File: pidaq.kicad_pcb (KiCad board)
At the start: 2 copper layers, 83.8 x 78.1 mm, 41 parts, among them J1 Screw_Terminal_01x08, J2 Screw_Terminal_01x08, J3 Screw_Terminal_01x10, J4 Screw_Terminal_01x10, J5 Conn_01x02_Male, J6 Conn_01x08_Female, U1 LTC2984CLX-DNP, U2 LTC2418IGN-DNP

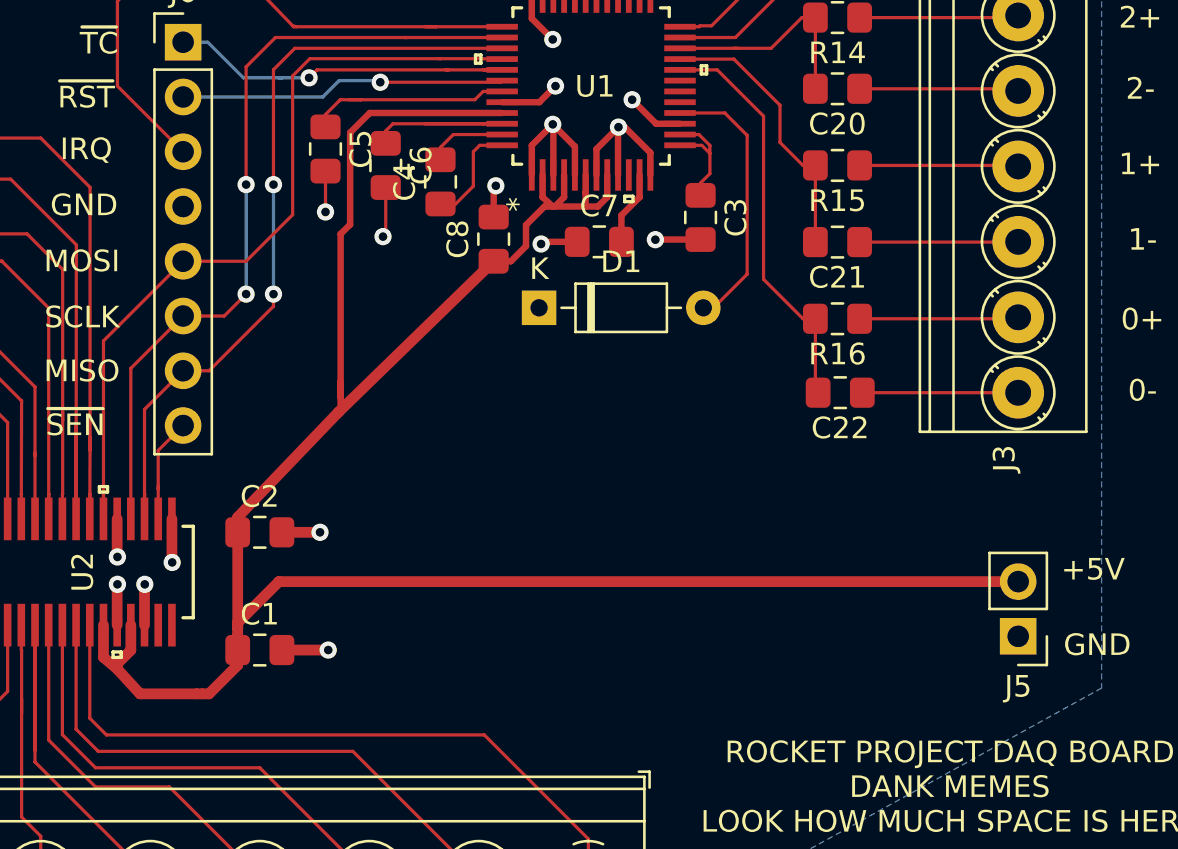
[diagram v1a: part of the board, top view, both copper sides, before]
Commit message: add level shifters to MISO
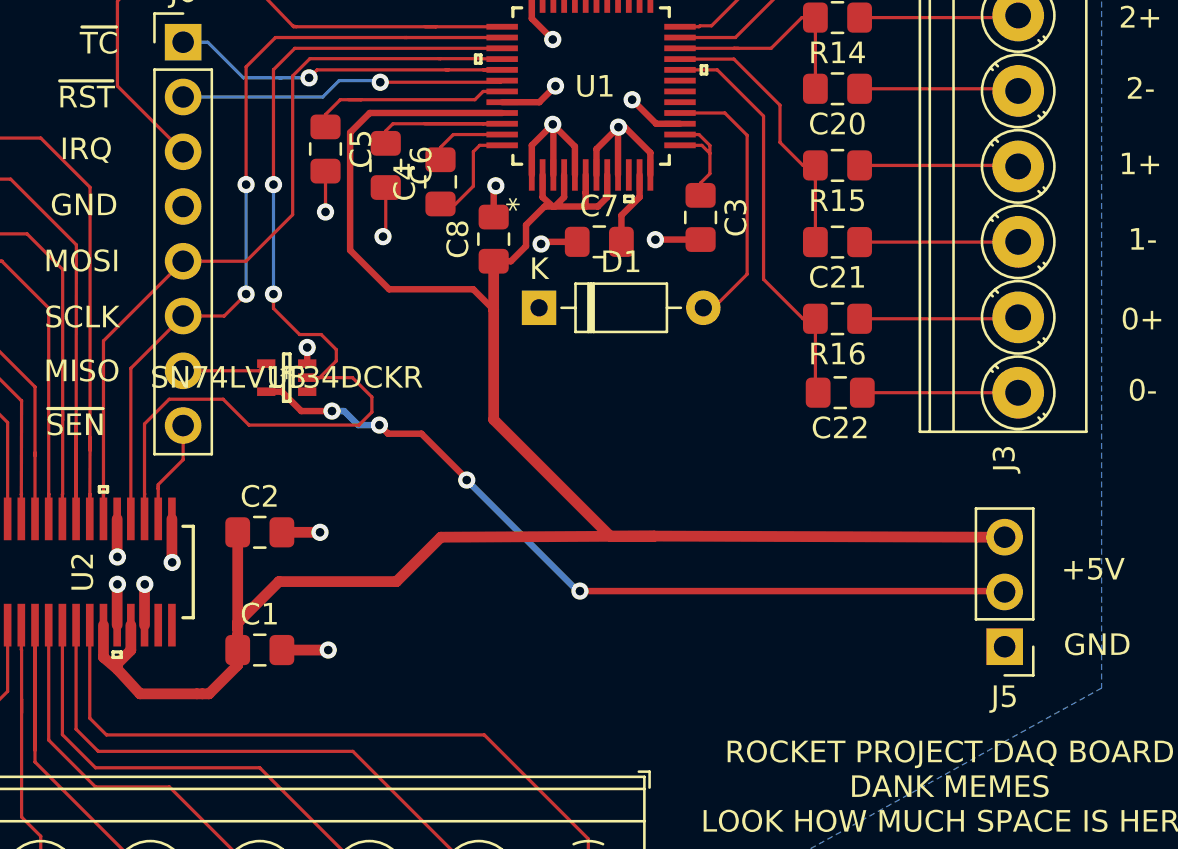
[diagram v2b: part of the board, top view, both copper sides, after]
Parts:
- added U3: SN74LV1T34DCKR, proj_footprints:SN74LV1T34DCKR, F.Cu at (117.2, 127.7)
- C2, C7, C8: value 0.1uF -> 100nF
- C4: value 10uF X7R -> 10uF
- C6: value 10uF X5R -> 10uF
- J5: value Conn_01x02_Male -> Conn_01x03_Male; footprint Connector_PinHeader_2.54mm:PinHeader_1x02_P2.54mm_Vertical -> Connector_PinHeader_2.54mm:PinHeader_1x03_P2.54mm_Vertical
- moved J5 0.79 mm to (150.5, 140.2)
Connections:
- J5 pad 2: +5V -> VDOUT
- J6 pad 7: MISO -> Net-(J6-Pad7)
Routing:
- net VDOUT: track 0.00 -> 38.8 mm, vias 0 -> 4
- net MISO: track 35.2 -> 48.3 mm
- net Net-(J6-Pad7): track 0.00 -> 3.99 mm
- net +5V: track 107.2 -> 105.5 mm
- net GND: track 116.4 -> 117.4 mm, vias 16 -> 17

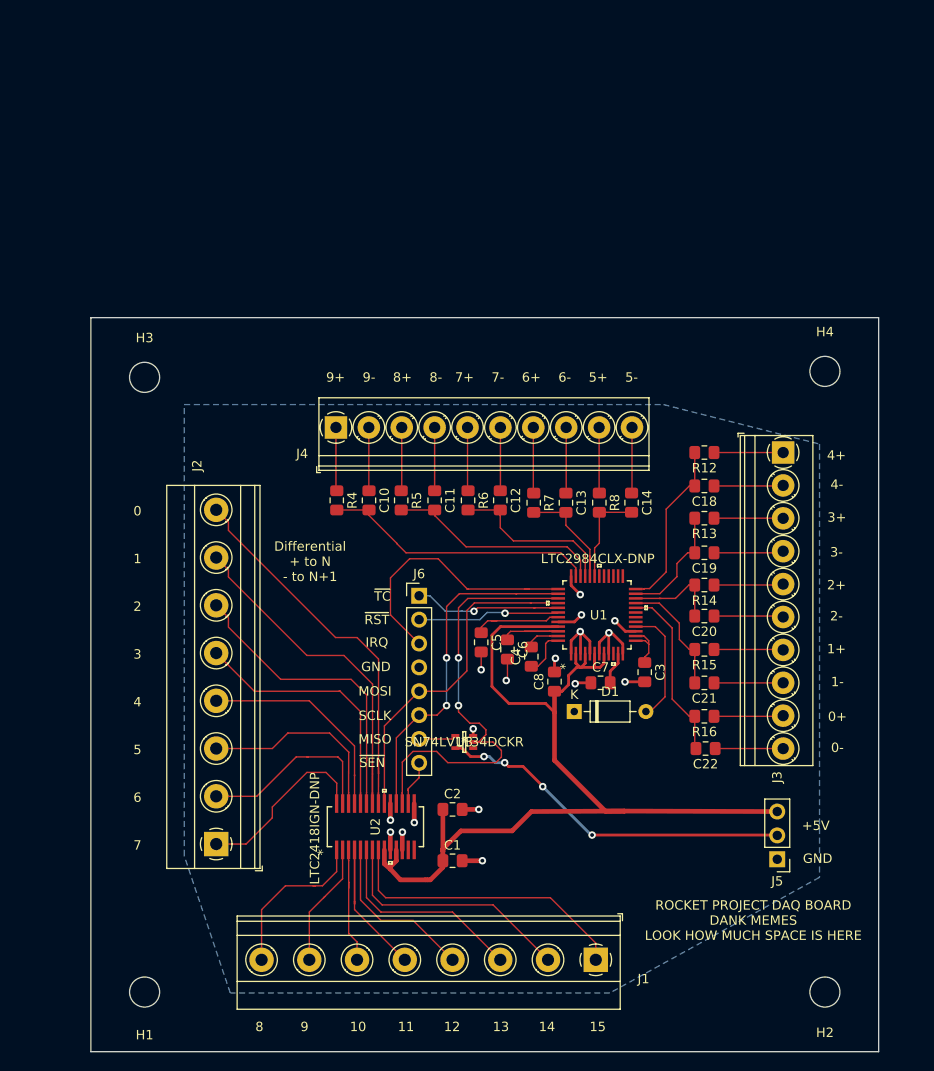
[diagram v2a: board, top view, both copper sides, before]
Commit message: reversed screw terminal symbols
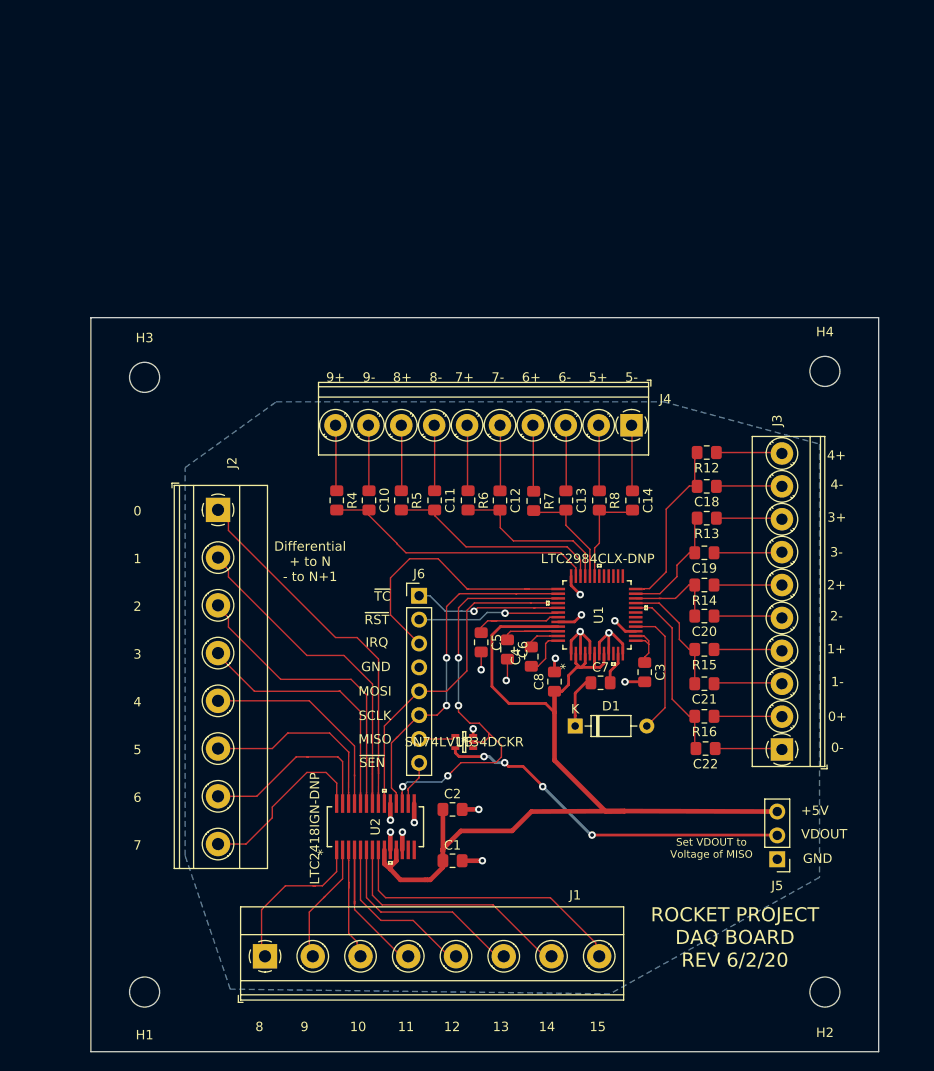
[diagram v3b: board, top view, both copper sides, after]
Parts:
- moved J2 35.6 mm to (91.0, 103.0), turned to 270 degrees
- moved J1 35.2 mm to (96.0, 150.5), turned to 0 degrees
- moved J3 31.6 mm to (151.0, 128.5), turned to 90 degrees
- moved J4 31.5 mm to (135.0, 94.0), turned to 180 degrees
- moved D1 1.54 mm to (129.0, 126.0)
- moved C18 0.26 mm to (143.0, 100.5)
- moved C14 0.26 mm to (135.1, 102.0)
- moved R12 0.25 mm to (143.0, 96.9)
- moved R13 0.25 mm to (143.0, 103.9)
- moved C13 0.24 mm to (128.0, 102.0)
- moved R8 0.23 mm to (131.6, 102.0)
- moved R7 0.19 mm to (124.6, 102.0)
- moved C21 0.09 mm to (142.7, 121.5)
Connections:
- net CS_SEN renamed ~SEN
- net CS_TC renamed ~TC
- net Net-(J6-Pad7) renamed /MISO_SAFE
- J1 pad 1: SEN15 -> Net-(J1-Pad1)
- J1 pad 2: SEN14 -> Net-(J1-Pad2)
- J1 pad 3: SEN13 -> Net-(J1-Pad3)
- J1 pad 4: SEN12 -> Net-(J1-Pad4)
- J1 pad 5: SEN11 -> Net-(J1-Pad5)
- J1 pad 6: SEN10 -> Net-(J1-Pad6)
- J1 pad 7: SEN9 -> Net-(J1-Pad7)
- J1 pad 8: SEN8 -> Net-(J1-Pad8)
- J2 pad 1: /SEN7 -> /SEN0
- J2 pad 2: /SEN6 -> /SEN1
- J2 pad 3: /SEN5 -> /SEN2
- J2 pad 4: /SEN4 -> /SEN3
- J2 pad 5: /SEN3 -> /SEN4
- J2 pad 6: /SEN2 -> /SEN5
- J2 pad 7: /SEN1 -> /SEN6
- J2 pad 8: /SEN0 -> /SEN7
- J3 pad 1: Net-(J3-Pad1) -> GND
- J3 pad 10: GND -> Net-(J3-Pad10)
- J3 pad 2: GND -> Net-(J3-Pad2)
- J3 pad 3: Net-(J3-Pad3) -> GND
- J3 pad 4: GND -> Net-(J3-Pad4)
- J3 pad 5: Net-(J3-Pad5) -> GND
- J3 pad 6: GND -> Net-(J3-Pad6)
- J3 pad 7: Net-(J3-Pad7) -> GND
- J3 pad 8: GND -> Net-(J3-Pad8)
- J3 pad 9: Net-(J3-Pad9) -> GND
- J4 pad 1: Net-(J4-Pad1) -> GND
- J4 pad 10: GND -> Net-(J4-Pad10)
- J4 pad 2: GND -> Net-(J4-Pad2)
- J4 pad 3: Net-(J4-Pad3) -> GND
- J4 pad 4: GND -> Net-(J4-Pad4)
- J4 pad 5: Net-(J4-Pad5) -> GND
- J4 pad 6: GND -> Net-(J4-Pad6)
- J4 pad 7: Net-(J4-Pad7) -> GND
- J4 pad 8: GND -> Net-(J4-Pad8)
- J4 pad 9: Net-(J4-Pad9) -> GND
- R12 pad 1: Net-(J3-Pad1) -> Net-(J3-Pad10)
- R13 pad 1: Net-(J3-Pad3) -> Net-(J3-Pad8)
- R14 pad 1: Net-(J3-Pad5) -> Net-(J3-Pad6)
- R15 pad 1: Net-(J3-Pad7) -> Net-(J3-Pad4)
- R16 pad 1: Net-(J3-Pad9) -> Net-(J3-Pad2)
- R4 pad 1: Net-(J4-Pad1) -> Net-(J4-Pad10)
- R5 pad 1: Net-(J4-Pad3) -> Net-(J4-Pad8)
- R6 pad 1: Net-(J4-Pad5) -> Net-(J4-Pad6)
- R7 pad 1: Net-(J4-Pad7) -> Net-(J4-Pad4)
- R8 pad 1: Net-(J4-Pad9) -> Net-(J4-Pad2)
- U2 pad 1: SEN8 -> Net-(J1-Pad1)
- U2 pad 2: SEN9 -> Net-(J1-Pad2)
- U2 pad 3: SEN10 -> Net-(J1-Pad3)
- U2 pad 4: SEN11 -> Net-(J1-Pad4)
- U2 pad 5: SEN12 -> Net-(J1-Pad5)
- U2 pad 6: SEN13 -> Net-(J1-Pad6)
- U2 pad 7: SEN14 -> Net-(J1-Pad7)
- U2 pad 8: SEN15 -> Net-(J1-Pad8)
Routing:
- net SEN15: track 31.5 -> 0.00 mm
- net Net-(J1-Pad8): track 0.00 -> 31.5 mm
- net SEN14: track 26.4 -> 0.00 mm
- net Net-(J1-Pad7): track 0.00 -> 26.4 mm
- net SEN13: track 22.1 -> 0.00 mm
- net Net-(J1-Pad6): track 0.00 -> 22.1 mm
- net SEN11: track 20.0 -> 0.00 mm
- net Net-(J1-Pad4): track 0.00 -> 20.0 mm
- net SEN12: track 17.8 -> 0.00 mm
- net Net-(J1-Pad5): track 0.00 -> 17.8 mm
- net SEN8: track 17.6 -> 0.00 mm
- net Net-(J1-Pad1): track 0.00 -> 17.6 mm
- net SEN9: track 13.3 -> 0.00 mm
- net Net-(J1-Pad2): track 0.00 -> 13.3 mm
- net SEN10: track 12.7 -> 0.00 mm
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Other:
- board text added: "ROCKET PROJECT DAQ BOARD REV 6/2/20"
- board text added: "Set VDOUT to Voltage of MISO"
- board text added: "VDOUT"
- board text removed: "ROCKET PROJECT DAQ BOARD DANK MEMES LOOK HOW MUCH SPACE IS HERE"

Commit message: turn screw holes into plated ones for more grounding
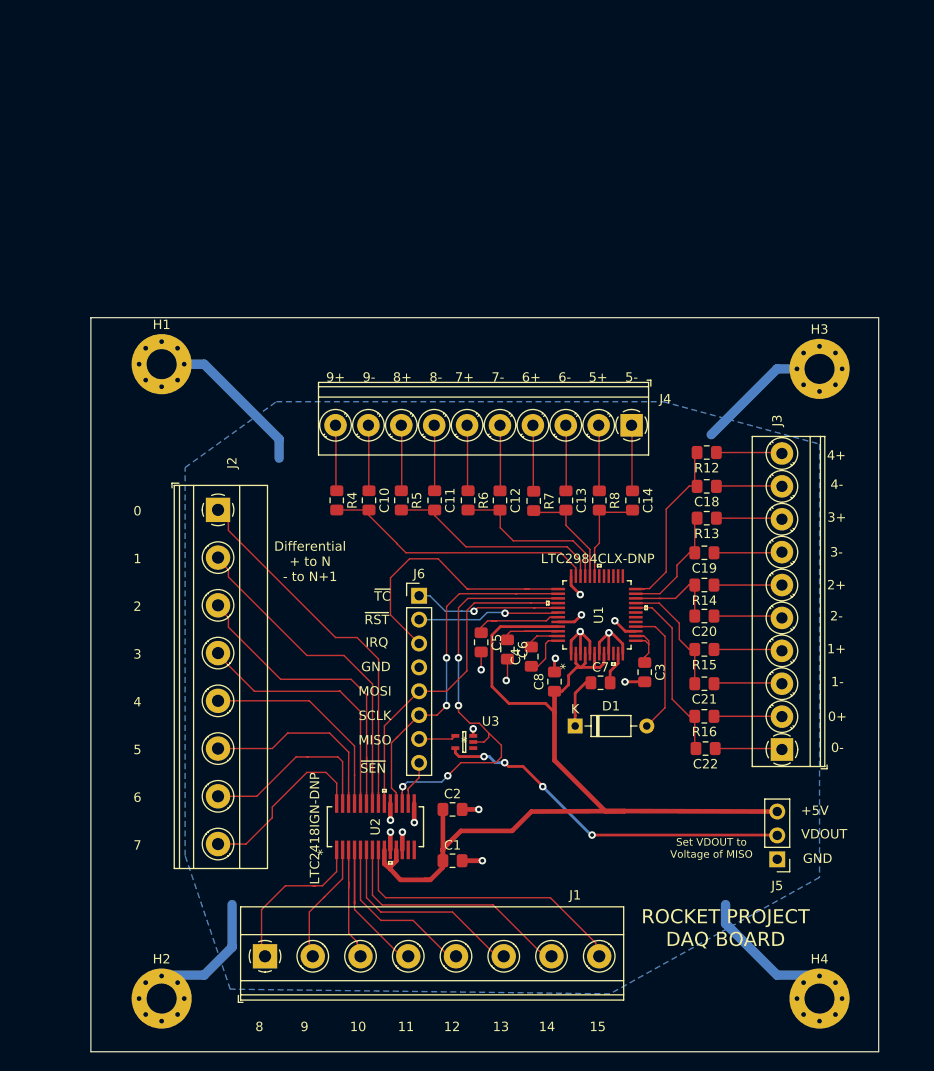
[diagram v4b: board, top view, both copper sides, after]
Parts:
- H1, H2, H3, H4: value MountingHole -> MountingHole_Pad; footprint MountingHole:MountingHole_3.2mm_M3 -> MountingHole:MountingHole_3.2mm_M3_Pad_Via
- moved H3 71.8 mm to (155.0, 88.0)
- moved H2 70.6 mm to (85.0, 155.0)
- moved H1 66.8 mm to (85.0, 87.5)
- moved H4 66.7 mm to (155.0, 155.0)
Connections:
- H1 pad 1: (no net) -> GND
- H2 pad 1: (no net) -> GND
- H3 pad 1: (no net) -> GND
- H4 pad 1: (no net) -> GND
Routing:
- net GND: track 121.3 -> 181.1 mm
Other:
- board text added: "ROCKET PROJECT DAQ BOARD"
- board text removed: "ROCKET PROJECT DAQ BOARD REV 6/2/20"

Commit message: completed design 2.0
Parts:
- removed C19, C20, C21, C22: 100pF, Capacitor_SMD:C_0805_2012Metric_Pad1.15x1.40mm_HandSolder
- removed R12, R13, R14, R15, R16: 100, Resistor_SMD:R_0805_2012Metric_Pad1.15x1.40mm_HandSolder
- added C15: 10uF, Capacitor_SMD:C_0805_2012Metric_Pad1.15x1.40mm_HandSolder, F.Cu at (105.2, 110.4)
- added C16: 10uF, Capacitor_SMD:C_0805_2012Metric_Pad1.15x1.40mm_HandSolder, F.Cu at (104.4, 107.1)
- added C17: 10uF, Capacitor_SMD:C_0805_2012Metric_Pad1.15x1.40mm_HandSolder, F.Cu at (128.1, 80.3)
- added C9: 100pF, Capacitor_SMD:C_0805_2012Metric_Pad1.15x1.40mm_HandSolder, F.Cu at (85.1, 124.5)
- added J7: Screw_Terminal_01x04, TerminalBlock_Phoenix:TerminalBlock_Phoenix_MKDS-1,5-4-5.08_1x04_P5.08mm_Horizontal, F.Cu at (133.3, 136.5)
- added J8: Conn_01x03_Male, Connector_PinHeader_2.54mm:PinHeader_1x03_P2.54mm_Vertical, F.Cu at (138.8, 111.6)
- added R1: 100, Resistor_SMD:R_0805_2012Metric_Pad1.15x1.40mm_HandSolder, F.Cu at (85.1, 92.7)
- added R10: 100, Resistor_SMD:R_0805_2012Metric_Pad1.15x1.40mm_HandSolder, F.Cu at (85.1, 106.7)
- added R2: 100, Resistor_SMD:R_0805_2012Metric_Pad1.15x1.40mm_HandSolder, F.Cu at (85.1, 87.6)
- added R3: 100, Resistor_SMD:R_0805_2012Metric_Pad1.15x1.40mm_HandSolder, F.Cu at (85.1, 82.5)
- added R9: 100, Resistor_SMD:R_0805_2012Metric_Pad1.15x1.40mm_HandSolder, F.Cu at (85.1, 111.8)
- added RG1: R_US, Resistor_THT:R_Axial_DIN0204_L3.6mm_D1.6mm_P7.62mm_Horizontal, F.Cu at (138.0, 120.8)
- added U4: INA126U, footprints:INA126U, F.Cu at (145.8, 124.8)
- C1: value 10uF -> 100nF
- C14: value 100pF -> 10uF
- C18: value 100pF -> 0.1uF
- C2: value 100nF -> 1uF
- C3: value 1uF -> 100nF
- C4, C5, C6: value 10uF -> 100pF
- C7, C8: value 100nF -> 100pF
- J1, J2: value Screw_Terminal_01x08 -> Screw_Terminal_01x10; footprint TerminalBlock_Phoenix:TerminalBlock_Phoenix_MKDS-1,5-8-5.08_1x08_P5.08mm_Horizontal -> TerminalBlock_Phoenix:TerminalBlock_Phoenix_MPT-0,5-10-2.54_1x10_P2.54mm_Horizontal
- J3, J4: value Screw_Terminal_01x10 -> Screw_Terminal_01x08; footprint TerminalBlock_Phoenix:TerminalBlock_Phoenix_PT-1,5-10-3.5-H_1x10_P3.50mm_Horizontal -> TerminalBlock_Phoenix:TerminalBlock_Phoenix_MKDS-1,5-8-5.08_1x08_P5.08mm_Horizontal
- U1: footprint proj_footprints:LTC2984CLX-PBF -> footprints:LTC2984CLX-PBF
- U2: value LTC2418IGN-DNP -> LTC2449CUHF; footprint proj_footprints:LTC2418IGN-PBF -> footprints:LTC2449CUHF
- U3: footprint proj_footprints:SN74LV1T34DCKR -> footprints:SN74LV1T34DCKR
- moved H2 122.5 mm to (158.8, 57.1)
- moved H4 80.3 mm to (76.2, 139.7)
- moved C8 66.2 mm to (85.1, 69.8), turned to 0 degrees
- moved C7 65.8 mm to (85.1, 74.9)
- moved U2 65.7 mm to (133.3, 76.2), turned to 180 degrees
- moved J1 60.3 mm to (78.7, 92.7), turned to 90 degrees
- moved D1 58.2 mm to (78.0, 98.0)
- moved J5 55.4 mm to (95.1, 139.4), turned to 90 degrees
- moved C6 52.7 mm to (85.1, 80.0), turned to 0 degrees
- moved H3 51.8 mm to (158.8, 139.7)
- moved R8 48.8 mm to (85.1, 116.8), turned to 0 degrees
- moved C4 48.5 mm to (85.1, 90.2), turned to 0 degrees
- moved C5 46.6 mm to (85.1, 85.1), turned to 0 degrees
- moved C1 44.8 mm to (107.8, 96.3), turned to 270 degrees
- moved R7 44.2 mm to (85.1, 121.9), turned to 0 degrees
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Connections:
- C1 pad 1: +5V -> GND
- C1 pad 2: GND -> Net-(C1-Pad2)
- C10 pad 2: TC9+ -> TC8+
- C11 pad 2: TC8+ -> TC7+
- C12 pad 2: TC7+ -> TC6+
- C13 pad 2: TC6+ -> TC5+
- C14 pad 1: GND -> Net-(C14-Pad1)
- C14 pad 2: TC5+ -> Net-(C14-Pad2)
- C18 pad 1: GND -> +5V
- C18 pad 2: TC4+ -> GND
- C2 pad 1: +5V -> Net-(C2-Pad1)
- C3 pad 1: Net-(C3-Pad1) -> +5V
- C4 pad 1: Net-(C4-Pad1) -> GND
- C4 pad 2: Net-(C4-Pad2) -> TC4+
- C5 pad 1: Net-(C5-Pad1) -> GND
- C5 pad 2: GND -> TC3+
- C6 pad 1: Net-(C6-Pad1) -> GND
- C6 pad 2: GND -> TC2+
- C7 pad 2: Net-(C7-Pad2) -> TC1+
- C8 pad 1: +5V -> GND
- C8 pad 2: GND -> TC0+
- D1 pad 2: Net-(D1-Pad2) -> /thermocouples/CJ
- J1 pad 1: Net-(J1-Pad1) -> /thermocouples/TC4RAW
- J1 pad 2: Net-(J1-Pad2) -> GND
- J1 pad 3: Net-(J1-Pad3) -> /thermocouples/TC3RAQ
- J1 pad 4: Net-(J1-Pad4) -> GND
- J1 pad 5: Net-(J1-Pad5) -> /thermocouples/TC2RAW
- J1 pad 6: Net-(J1-Pad6) -> GND
- J1 pad 7: Net-(J1-Pad7) -> /thermocouples/TC1RAW
- J1 pad 8: Net-(J1-Pad8) -> GND
- J2 pad 1: /SEN0 -> /thermocouples/TC9RAW
- J2 pad 2: /SEN1 -> GND
- J2 pad 3: /SEN2 -> /thermocouples/TC8RAW
- J2 pad 4: /SEN3 -> GND
- J2 pad 5: /SEN4 -> /thermocouples/TC7RAW
- J2 pad 6: /SEN5 -> GND
- J2 pad 7: /SEN6 -> /thermocouples/TC6RAW
- J2 pad 8: /SEN7 -> GND
- J3 pad 1: GND -> SEN0
- J3 pad 2: Net-(J3-Pad2) -> SEN1
- J3 pad 3: GND -> SEN2
- J3 pad 4: Net-(J3-Pad4) -> SEN3
- J3 pad 5: GND -> SEN4
- J3 pad 6: Net-(J3-Pad6) -> SEN5
- J3 pad 7: GND -> SEN6
- J3 pad 8: Net-(J3-Pad8) -> SEN7
- J4 pad 1: GND -> SEN8
- J4 pad 2: Net-(J4-Pad2) -> SEN9
- J4 pad 3: GND -> SEN10
- J4 pad 4: Net-(J4-Pad4) -> SEN11
- J4 pad 5: GND -> SEN12
- J4 pad 6: Net-(J4-Pad6) -> SEN13
- J4 pad 7: GND -> SEN14
- J4 pad 8: Net-(J4-Pad8) -> SEN15
- J6 pad 1: ~TC -> ~SEN
- J6 pad 2: RST -> ~TC
- J6 pad 3: IRQ -> ~RST
- J6 pad 4: GND -> IRQ
- J6 pad 5: MOSI -> GND
- J6 pad 6: SCLK -> MOSI
- J6 pad 7: /MISO_SAFE -> SCLK
- J6 pad 8: ~SEN -> /MISO_SAFE
- R4 pad 1: Net-(J4-Pad10) -> /thermocouples/TC1RAW
- R4 pad 2: TC9+ -> TC1+
- R5 pad 1: Net-(J4-Pad8) -> /thermocouples/TC0RAW
- R5 pad 2: TC8+ -> TC0+
- R6 pad 1: Net-(J4-Pad6) -> /thermocouples/TC9RAW
- R6 pad 2: TC7+ -> TC9+
- R7 pad 1: Net-(J4-Pad4) -> /thermocouples/TC8RAW
- R7 pad 2: TC6+ -> TC8+
- R8 pad 1: Net-(J4-Pad2) -> /thermocouples/TC7RAW
- R8 pad 2: TC5+ -> TC7+
- U1 pad 11: Net-(C7-Pad2) -> Net-(C1-Pad2)
- U1 pad 13: Net-(C3-Pad1) -> Net-(C2-Pad1)
- U1 pad 14: Net-(C3-Pad1) -> Net-(C2-Pad1)
- U1 pad 16: Net-(D1-Pad2) -> (no net)
- U1 pad 27: (no net) -> /thermocouples/CJ
- U1 pad 42: RST -> ~RST
- U1 pad 43: Net-(C5-Pad1) -> Net-(C15-Pad1)
- U1 pad 46: Net-(C6-Pad1) -> Net-(C16-Pad1)
- U1 pad 47: Net-(C4-Pad2) -> Net-(C14-Pad2)
- U1 pad 48: Net-(C4-Pad1) -> Net-(C14-Pad1)
- U2 pad 1: Net-(J1-Pad1) -> GND
- U2 pad 10: GND -> SEN2
- U2 pad 11: +5V -> SEN3
- U2 pad 12: GND -> SEN4
- U2 pad 13: (no net) -> SEN5
- U2 pad 14: (no net) -> SEN6
- U2 pad 15: GND -> SEN7
- U2 pad 16: ~SEN -> SEN8
- U2 pad 17: MISO -> SEN9
- U2 pad 18: SCLK -> SEN10
- U2 pad 19: GND -> SEN11
- U2 pad 2: Net-(J1-Pad2) -> (no net)
- U2 pad 20: MOSI -> SEN12
- U2 pad 21: /SEN0 -> SEN13
- U2 pad 22: /SEN1 -> SEN14
- U2 pad 23: /SEN2 -> SEN15
- U2 pad 24: /SEN3 -> (no net)
- U2 pad 25: /SEN4 -> (no net)
- U2 pad 26: /SEN5 -> (no net)
- U2 pad 27: /SEN6 -> (no net)
- U2 pad 28: /SEN7 -> +5V
- U2 pad 3: Net-(J1-Pad3) -> GND
- U2 pad 4: Net-(J1-Pad4) -> GND
- U2 pad 5: Net-(J1-Pad5) -> GND
- U2 pad 6: Net-(J1-Pad6) -> GND
- U2 pad 7: Net-(J1-Pad7) -> GND
- U2 pad 8: Net-(J1-Pad8) -> SEN0
- U2 pad 9: +5V -> SEN1
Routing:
- net SEN0: track 0.00 -> 55.9 mm
- net SEN1: track 0.00 -> 46.4 mm
- net SCLK: track 37.5 -> 81.0 mm
- net SEN2: track 0.00 -> 42.6 mm
- net +EXC: track 0.00 -> 42.6 mm
- net /SEN0: track 41.5 -> 0.00 mm
- net MISO: track 46.0 -> 87.0 mm
- net /SEN1: track 41.0 -> 0.00 mm
- net SEN15: track 0.00 -> 40.1 mm
- net +5V: track 105.5 -> 144.2 mm, vias 0 -> 2
- net SEN3: track 0.00 -> 38.7 mm
- net SEN5: track 0.00 -> 36.9 mm
- net SEN14: track 0.00 -> 34.8 mm
- net SEN4: track 0.00 -> 34.5 mm
- net ~RST: track 0.00 -> 34.5 mm
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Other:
- board size 83.8 x 78.1 mm -> 95.2 x 95.3 mm
- board text removed: "+5V"
- board text removed: "0"
- board text removed: "0+"
- board text removed: "0-"
- board text removed: "1"
- board text removed: "1+"
- board text removed: "1-"
- board text removed: "10"
- board text removed: "11"
- board text removed: "12"
- board text removed: "13"
- board text removed: "14"
- board text removed: "15"
- board text removed: "2"
- board text removed: "2+"
- board text removed: "2-"
- board text removed: "3"
- board text removed: "3+"
- board text removed: "3-"
- board text removed: "4"
- board text removed: "4+"
- board text removed: "4-"
- board text removed: "5"
- board text removed: "5+"
- board text removed: "5-"
- board text removed: "6"
- board text removed: "6+"
- board text removed: "6-"
- board text removed: "7"
- board text removed: "7+"
- board text removed: "7-"
- board text removed: "8"
- board text removed: "8+"
- board text removed: "8-"
- board text removed: "9"
- board text removed: "9+"
- board text removed: "9-"
- board text removed: "Differential + to N - to N+1"
- board text removed: "GND"
- board text removed: "IRQ"
- board text removed: "MISO"
- board text removed: "MOSI"
- board text removed: "ROCKET PROJECT DAQ BOARD"
- board text removed: "SCLK"
- board text removed: "Set VDOUT to Voltage of MISO"
- board text removed: "VDOUT"
- board text removed: "~RST"
- board text removed: "~SEN"
- board text removed: "~TC"

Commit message: updated silkscreen and removed old adc
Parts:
- moved D1 5.75 mm to (83.7, 97.4)
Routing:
- net /thermocouples/CJ: track 9.94 -> 4.62 mm
- net +5V: track 144.2 -> 145.0 mm
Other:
- board text added: "+5V"
- board text added: "+EXC"
- board text added: "0"
- board text added: "0+"
- board text added: "0-"
- board text added: "1"
- board text added: "1+"
- board text added: "1-"
- board text added: "10"
- board text added: "11"
- board text added: "12"
- board text added: "13"
- board text added: "14"
- board text added: "15"
- board text added: "2"
- board text added: "2+"
- board text added: "2-"
- board text added: "3"
- board text added: "3+"
- board text added: "3-"
- board text added: "4"
- board text added: "4+"
- board text added: "4-"
- board text added: "5"
- board text added: "5+"
- board text added: "5-"
- board text added: "6"
- board text added: "6+"
- board text added: "6-"
- board text added: "7"
- board text added: "7+"
- board text added: "7-"
- board text added: "8"
- board text added: "8+"
- board text added: "8-"
- board text added: "9"
- board text added: "9+"
- board text added: "9-"
- board text added: "GND"
- board text added: "Jump LC to SEN0 To read Load Cell"
- board text added: "LC"
- board text added: "LC+"
- board text added: "LC-"
- board text added: "SEN0"
- board text added: "VDO"
